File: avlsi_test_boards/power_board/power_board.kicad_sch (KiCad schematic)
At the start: 9 parts, among them J1 PJ-102AH, J10 Conn_02x07_Odd_Even, J2 PJ-102AH, J3 Conn_02x07_Odd_Even, J4 Conn_02x07_Odd_Even, J9 Conn_02x07_Odd_Even

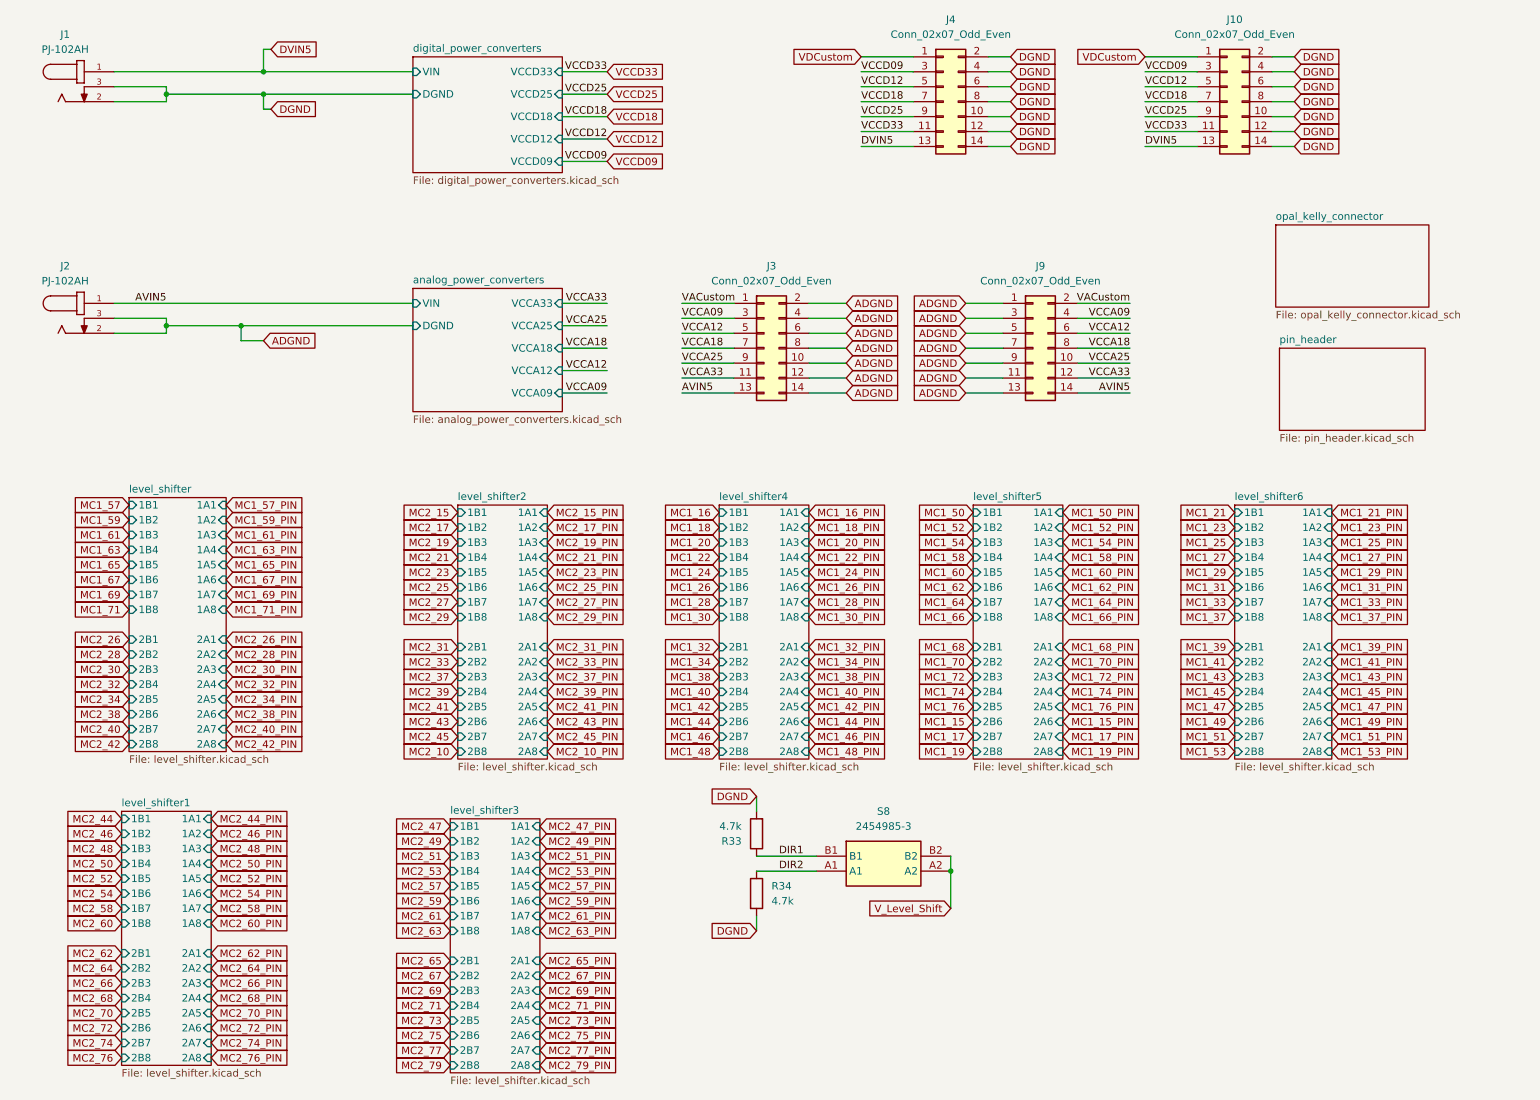
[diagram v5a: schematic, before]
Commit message: Update schematic and initial layout for pcb
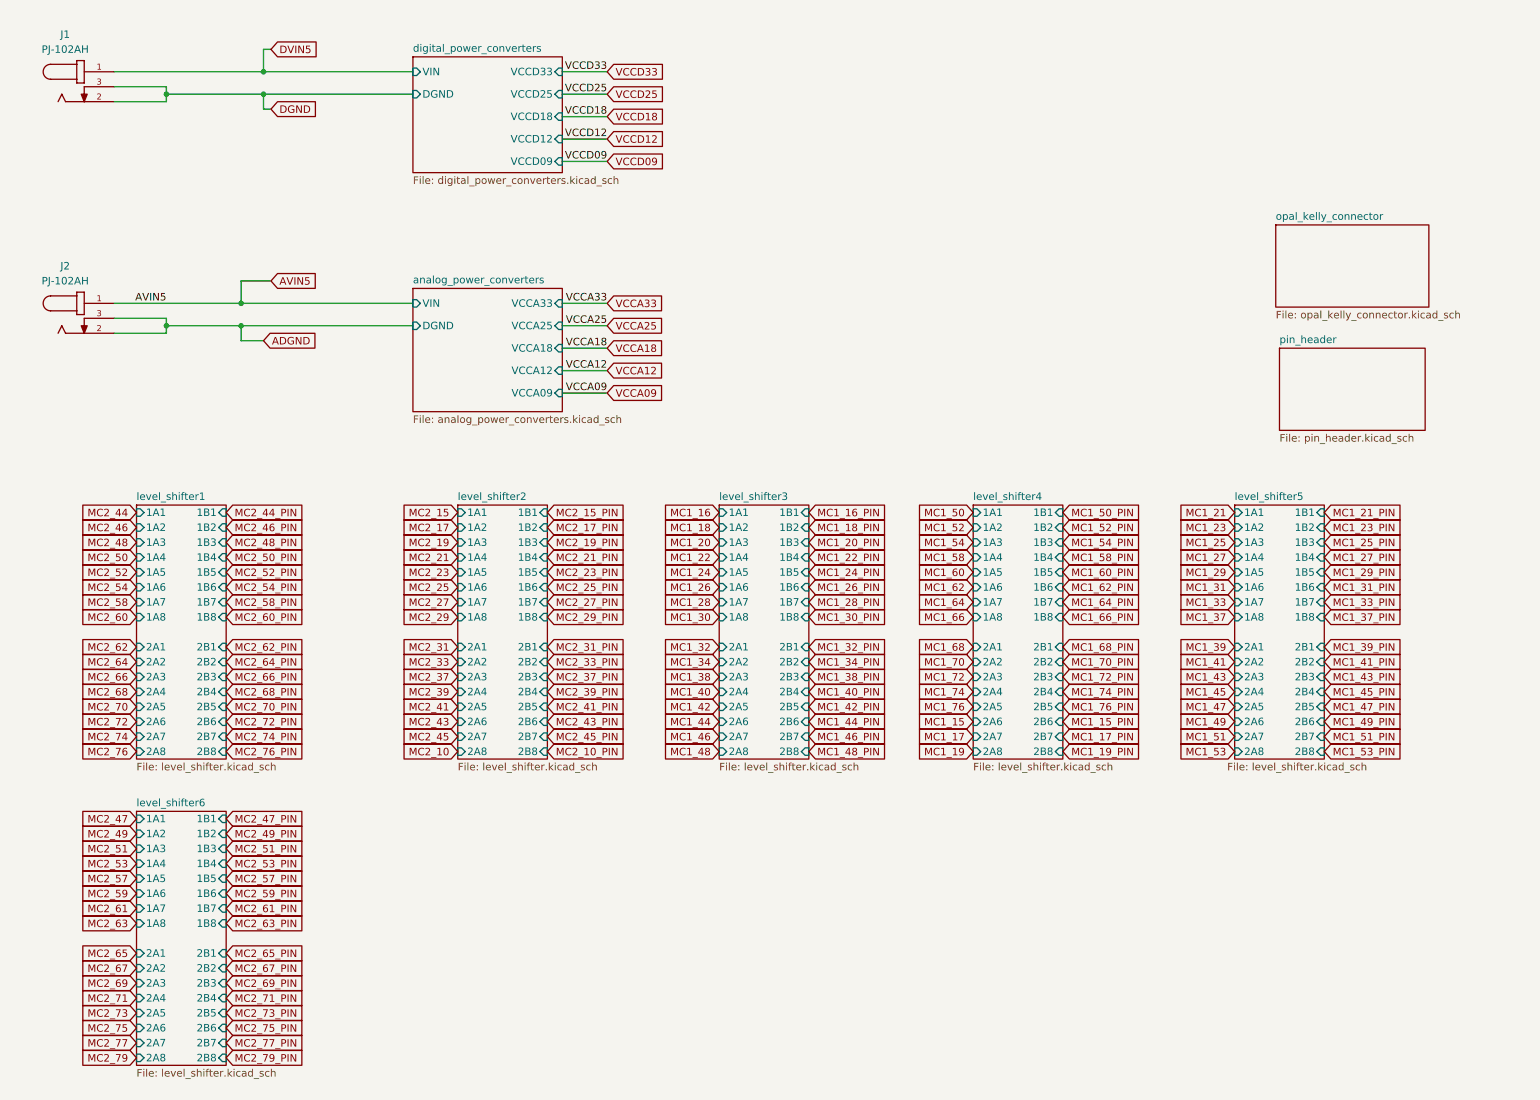
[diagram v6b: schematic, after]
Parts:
- removed J10, J3, J4, J9: Conn_02x07_Odd_Even, Connector_PinHeader_2.54mm:PinHeader_2x07_P2.54mm_Vertical, symbol Connector_Generic:Conn_02x07_Odd_Even
- removed R33, R34: 4.7k, Resistor_SMD:R_0805_2012Metric, symbol Device:R
- removed S8: 2454985-3, 2_DS:24549853, symbol 2_DIP:2454985-3
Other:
- removed sheet level_shifter

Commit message: Update schematic
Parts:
- removed J1, J2: PJ-102AH, Connector_BarrelJack:BarrelJack_CUI_PJ-102AH_Horizontal, symbol AVLSI:PJ-102AH
- added J1, J2: Conn_01x02_Pin, Connector_PinHeader_2.54mm:PinHeader_1x02_P2.54mm_Horizontal, symbol Connector:Conn_01x02_Pin
- added J3, J4: 2171750001, avlsi_preferred_parts:MOLEX_2171750001, symbol avlsi_preferred_parts:2171750001
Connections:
- net AVIN5: now also J2.2 (Pin_2), J4.A9 (VBUS1), J4.B9 (VBUS2)
- net DGND: now also J1.1 (Pin_1), J3.A12 (GND1), J3.A5 (CC1), J3.B12 (GND2), J3.B5 (CC2), J3.SH1 (SHIELD1), J3.SH2 (SHIELD2), J3.SH3 (SHIELD3), J3.SH4 (SHIELD4)
- net DVIN5: now also J1.2 (Pin_2), J3.A9 (VBUS1), J3.B9 (VBUS2)
- new net AGND: J2.1 (Pin_1), J4.A12 (GND1), J4.A5 (CC1), J4.B12 (GND2), J4.B5 (CC2), J4.SH1 (SHIELD1), J4.SH2 (SHIELD2), J4.SH3 (SHIELD3), J4.SH4 (SHIELD4)
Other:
- removed sheet level_shifter1
- removed sheet level_shifter2
- removed sheet level_shifter3
- removed sheet level_shifter4
- removed sheet level_shifter5
- removed sheet level_shifter6
- added sheet level_shifters (level_shifters.kicad_sch)
